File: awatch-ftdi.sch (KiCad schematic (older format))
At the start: 42 parts

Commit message: annotate all
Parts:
- gave numbers to parts that had none: 42

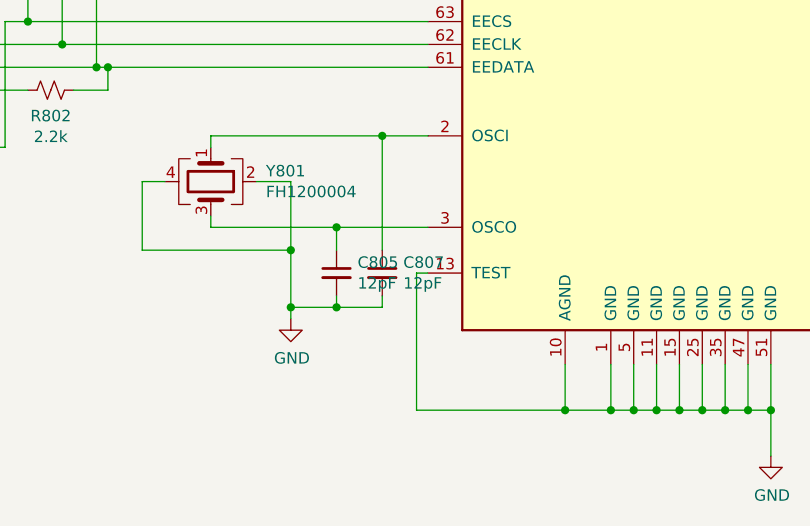
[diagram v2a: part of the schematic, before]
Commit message: update xtal caps on FTDI
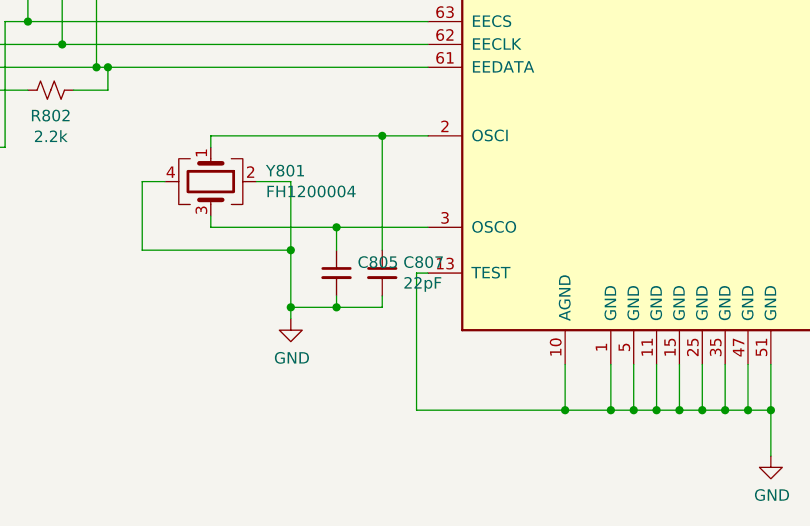
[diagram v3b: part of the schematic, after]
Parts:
- C805: value 12pF -> 22pF 22pF
- C807: value 12pF -> 22pF
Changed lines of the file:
@@
 P 4150 6250
 F 0 "C805" H 4242 6296 50  0000 L CNN
-F 1 "12pF" H 4242 6205 50  0000 L CNN
+F 1 "22pF 22pF" H 4242 6205 50  0000 L CNN
 F 2 "" H 4150 6250 50  0001 C CNN
 F 3 "~" H 4150 6250 50  0001 C CNN
@@
 P 4350 6250
 F 0 "C807" H 4442 6296 50  0000 L CNN
-F 1 "12pF" H 4442 6205 50  0000 L CNN
+F 1 "22pF" H 4442 6205 50  0000 L CNN
 F 2 "" H 4350 6250 50  0001 C CNN
 F 3 "~" H 4350 6250 50  0001 C CNN

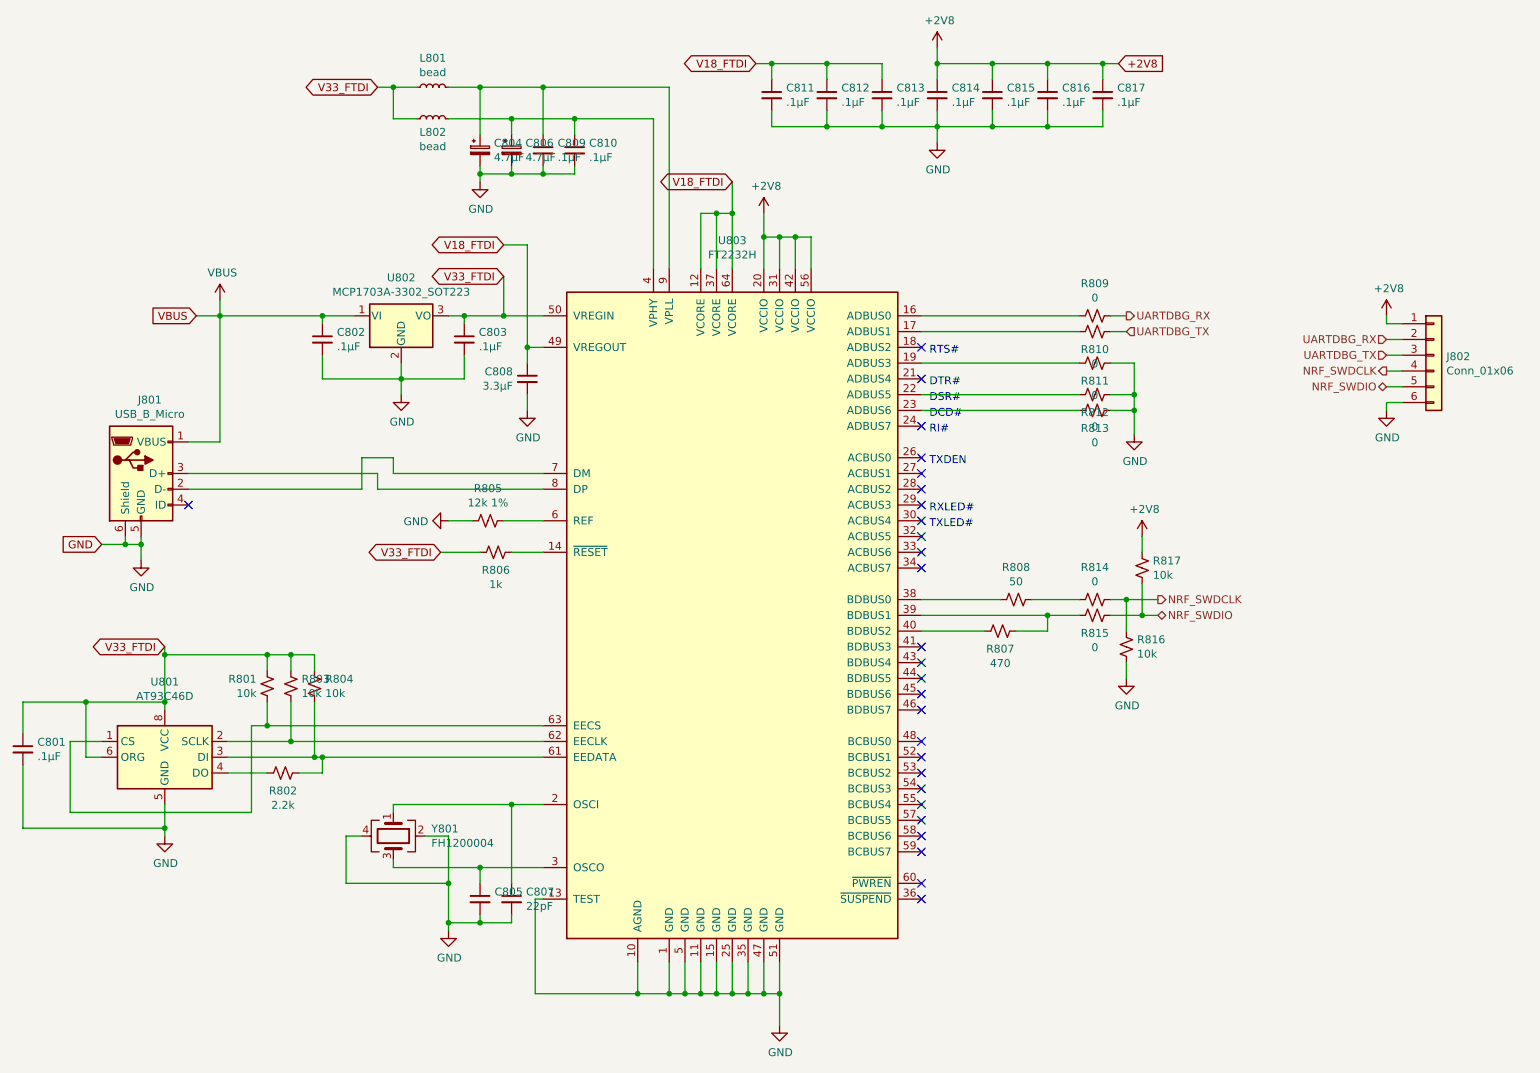
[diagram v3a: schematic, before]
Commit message: Add footprints.
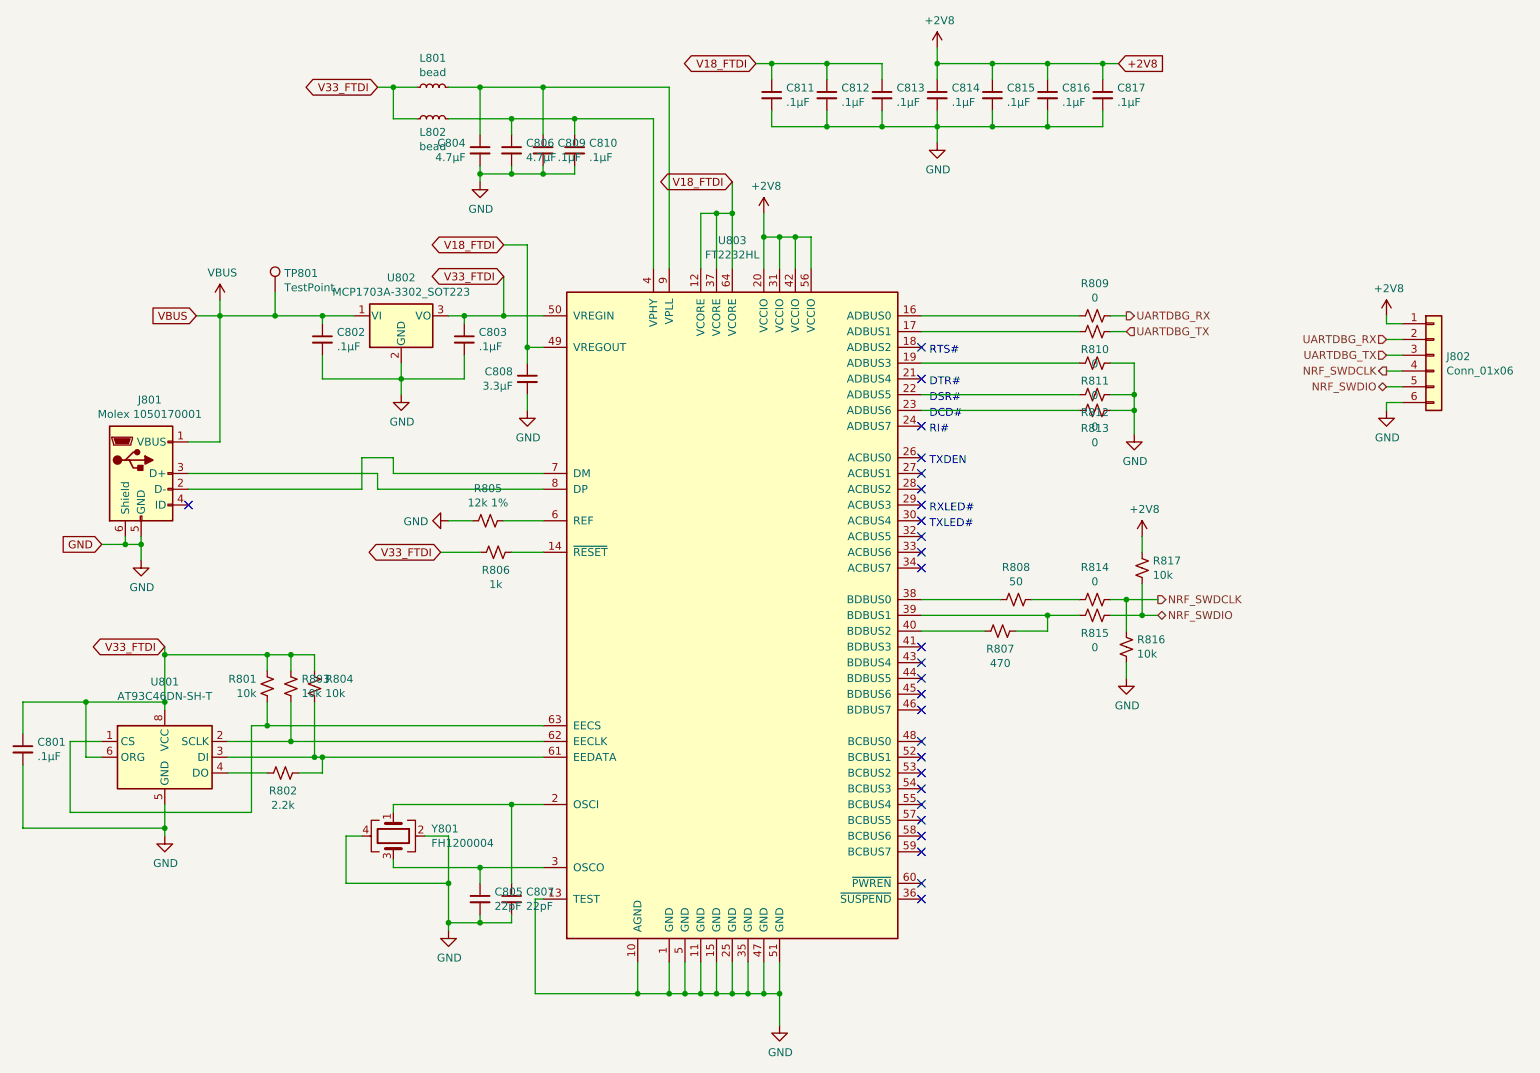
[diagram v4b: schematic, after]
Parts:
- removed C804, C806: 4.7µF, symbol Device:CP_Small
- added C804, C806: 4.7µF, Capacitor_SMD:C_0603_1608Metric, symbol Device:C_Small
- added TP801: TestPoint, TestPoint:TestPoint_Pad_D1.5mm, symbol Connector:TestPoint
- C801, C802, C803, C807, C808, C809, C810, C811, C812, C813, C814, C815, C816, C817: footprint (none) -> Capacitor_SMD:C_0603_1608Metric
- C805: value 22pF 22pF -> 22pF; footprint (none) -> Capacitor_SMD:C_0603_1608Metric
- J801: value USB_B_Micro -> Molex 1050170001; footprint (none) -> Connector_USB:USB_Micro-B_Molex-105017-0001
- J802: footprint (none) -> Connector_PinSocket_2.54mm:PinSocket_1x06_P2.54mm_Vertical
- L801, L802: footprint (none) -> Inductor_SMD:L_0603_1608Metric
- R801, R802, R803, R804, R805, R806, R807, R808, R809, R810, R811, R812, R813, R814, R815, R816, R817: footprint (none) -> Resistor_SMD:R_0603_1608Metric
- U801: value AT93C46D -> AT93C46DN-SH-T; footprint (none) -> Package_SO:SOIC-8_3.9x4.9mm_P1.27mm
- U803: value FT2232H -> FT2232HL; footprint (none) -> Package_QFP:LQFP-64_10x10mm_P0.5mm
- Y801: footprint (none) -> Crystal:Crystal_SMD_2520-4Pin_2.5x2.0mm
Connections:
- net GND: now also C804.2, C806.2
- net VBUS: now also TP801.1
- net at C810.1, L802.2, U803.4 (VPHY): now also C806.1
- net at C809.1, L801.2, U803.9 (VPLL): now also C804.1

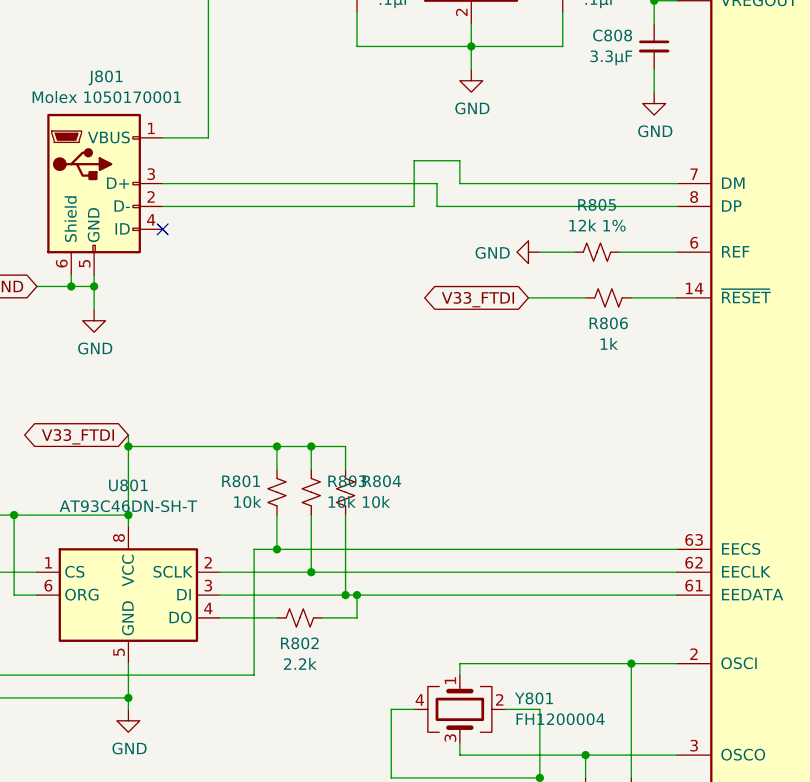
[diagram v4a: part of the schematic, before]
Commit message: FTDI placement
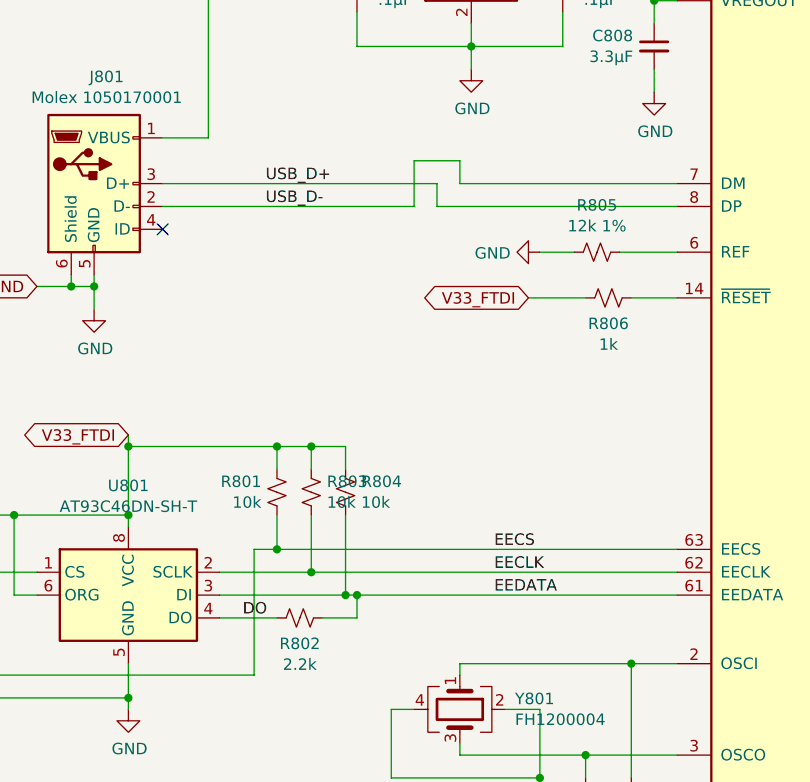
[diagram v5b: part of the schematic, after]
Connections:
- net EEDATA: now reaches R802.1, R804.1, U801.3 (DI), U803.61 (EEDATA)
- net EECLK: now reaches R803.1, U801.2 (SCLK), U803.62 (EECLK)
- net EECS: now reaches R801.1, U801.1 (CS), U803.63 (EECS)
- net USB_D-: now reaches J801.2 (D-), U803.7 (DM)
- net USB_D+: now reaches J801.3 (D+), U803.8 (DP)
- net DO: now reaches R802.2, U801.4 (DO)
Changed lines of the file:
@@
 	1    0    0    -1
 $EndComp
+Text Label 2750 3550 0    50   ~ 0
+USB_D+
+Text Label 2750 3650 0    50   ~ 0
+USB_D-
+Text Label 3750 5150 0    50   ~ 0
+EECS
+Text Label 3750 5250 0    50   ~ 0
+EECLK
+Text Label 3750 5350 0    50   ~ 0
+EEDATA
+Text Label 2650 5450 0    50   ~ 0
+DO
 $EndSCHEMATC

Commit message: Route FTDI.
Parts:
- added C818: .1µF, Capacitor_SMD:C_0603_1608Metric, symbol Device:C_Small
- J802: footprint Connector_PinSocket_2.54mm:PinSocket_1x06_P2.54mm_Vertical -> Connector_PinHeader_2.54mm:PinHeader_1x06_P2.54mm_Vertical
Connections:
- net GND: now also C818.2
- net V33_FTDI: now also C818.1
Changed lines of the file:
@@
 F 0 "J802" H 10280 2792 50  0000 L CNN
 F 1 "Conn_01x06" H 10280 2701 50  0000 L CNN
-F 2 "Connector_PinSocket_2.54mm:PinSocket_1x06_P2.54mm_Vertical" H 10200 2800 50  0001 C CNN
+F 2 "Connector_PinHeader_2.54mm:PinHeader_1x06_P2.54mm_Vertical" H 10200 2800 50  0001 C CNN
 F 3 "~" H 10200 2800 50  0001 C CNN
 	1    10200 2800
@@
 Wire Wire Line
 	2500 3350 2500 2550
-Wire Wire Line
-	2500 2550 2850 2550
 Connection ~ 3150 2550
 $Comp
@@
 	2850 2400 2850 2550
 Connection ~ 2850 2550
-Wire Wire Line
-	2850 2550 3150 2550
 $Comp
 L Device:C_Small C804
@@
 Text Label 2650 5450 0    50   ~ 0
 DO
+Wire Wire Line
+	2850 2550 3150 2550
+Wire Wire Line
+	2500 2550 2850 2550
+$Comp
+L Device:C_Small C818
+U 1 1 5C2F6C15
+P 4300 2700
+F 0 "C818" H 4392 2746 50  0000 L CNN
+F 1 ".1µF" H 4392 2655 50  0000 L CNN
+F 2 "Capacitor_SMD:C_0603_1608Metric" H 4300 2700 50  0001 C CNN
+F 3 "~" H 4300 2700 50  0001 C CNN
+	1    4300 2700
+	1    0    0    -1
+$EndComp
+Wire Wire Line
+	4300 2550 4300 2600
+Wire Wire Line
+	4300 2800 4300 2950
+Wire Wire Line
+	4300 2950 4050 2950
+Connection ~ 4050 2950
 $EndSCHEMATC
